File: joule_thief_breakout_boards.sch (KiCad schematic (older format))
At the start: 18 parts, among them J1 Conn_01x02, J10 Conn_01x02, J2 Conn_01x02, J3 Conn_01x02, J4 Conn_01x02, J5 Conn_01x02, J6 Conn_01x03, J7 Conn_01x03, J8 Conn_01x03, J9 Conn_01x02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

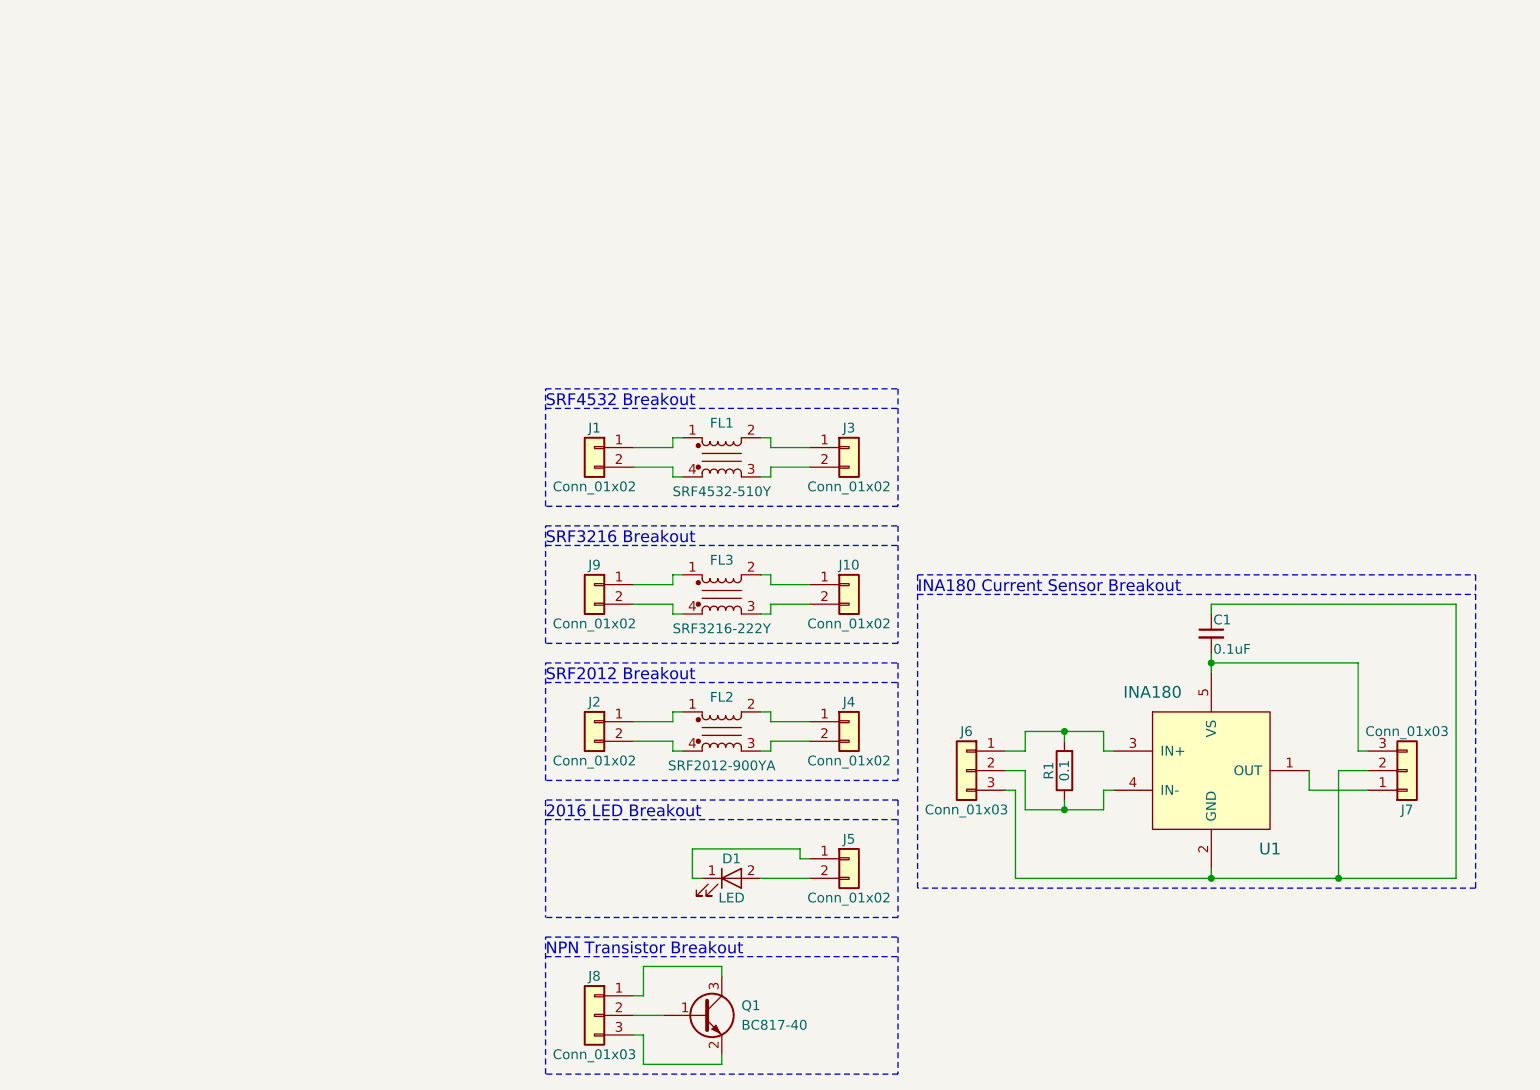
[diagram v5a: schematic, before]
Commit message: add complete joule thief with measurements sensors
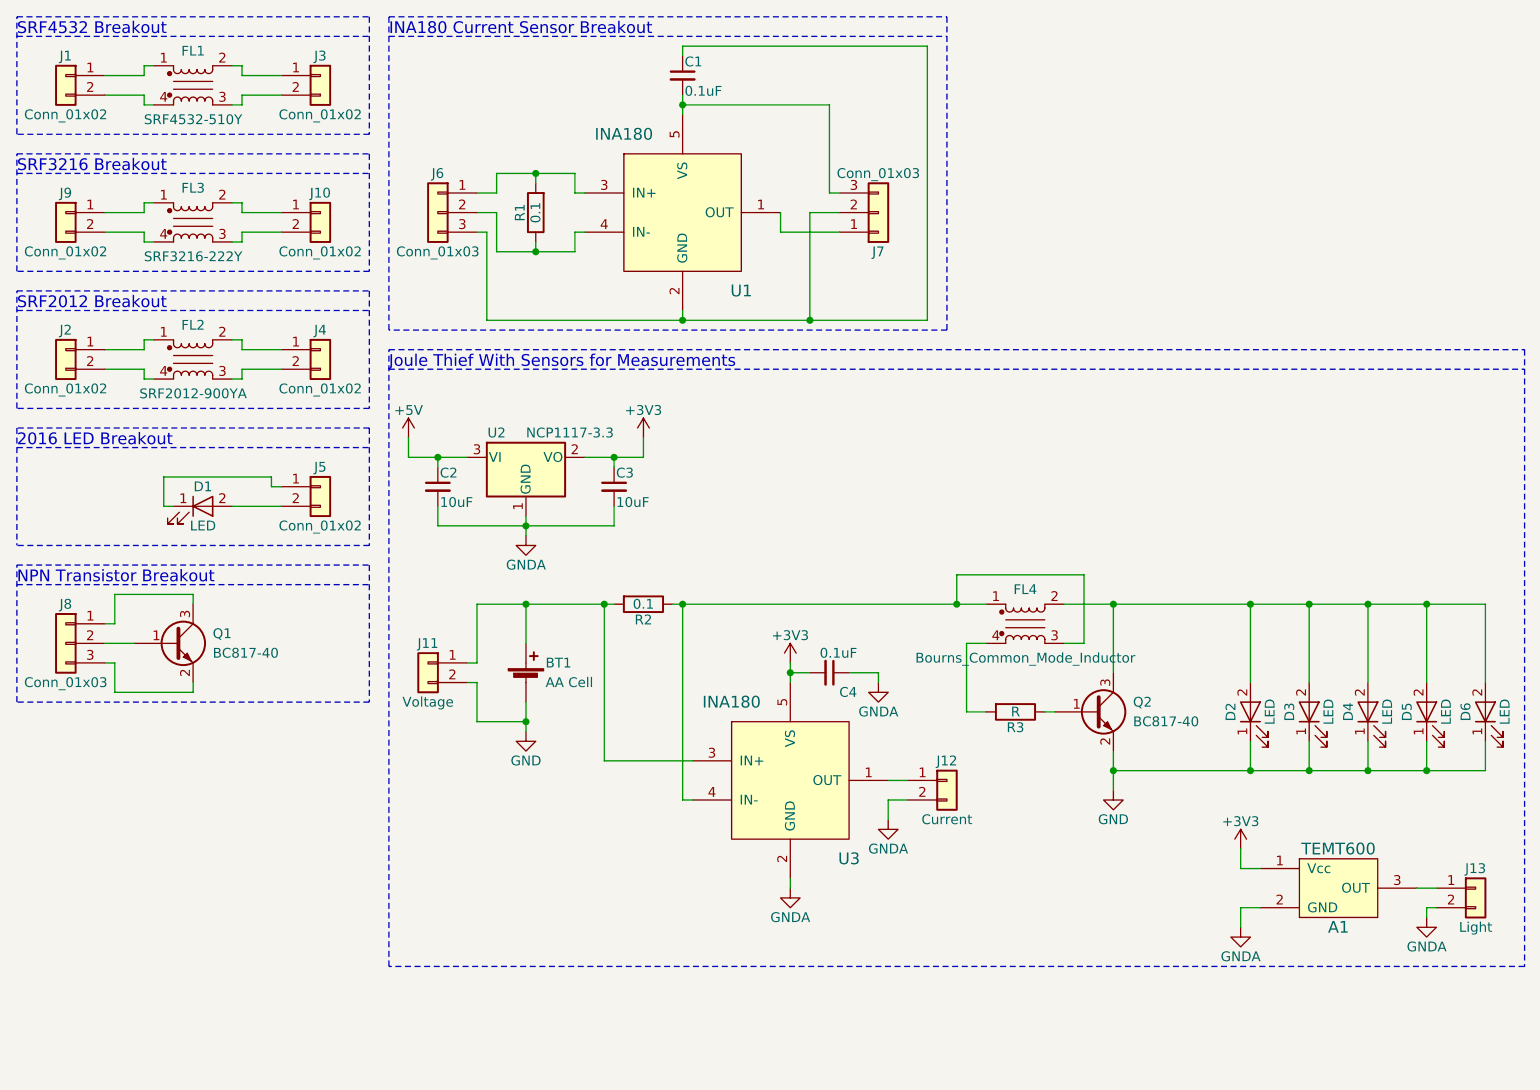
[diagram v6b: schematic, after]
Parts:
- added A1: TEMT600, symbol TEMT600
- added BT1: AA Cell, symbol Battery_Cell
- added C2, C3: 10uF, symbol C_Small
- added C4: 0.1uF, symbol C_Small
- added D2, D3, D4, D5, D6: LED, symbol LED
- added FL4: Bourns_Common_Mode_Inductor, symbol Bourns_Common_Mode_Inductor
- added J11: Voltage, symbol Conn_01x02
- added J12: Current, symbol Conn_01x02
- added J13: Light, symbol Conn_01x02
- added Q2: BC817-40, symbol Q_NPN_BEC
- added R2: 0.1, symbol R
- added R3: R, symbol R
- added U2: NCP1117-3.3, TO_SOT_Packages_SMD:TO-252-2, symbol NCP1117-3.3_TO252
- added U3: INA180, symbol INA180
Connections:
- new net: BT1.1 (+), J11.1 (Pin_1), R2.2, U3.3 (IN+)
- new net: FL4.1, FL4.3, R2.1, U3.4 (IN-)
- new net: D2.2 (A), D3.2 (A), D4.2 (A), D5.2 (A), D6.2 (A), FL4.2, Q2.3 (C)
- new net: FL4.4, R3.2
- new net: Q2.1 (B), R3.1
- new net: J12.1 (Pin_1), U3.1 (OUT)
- new net: A1.3 (OUT), J13.1 (Pin_1)
- new net +3V3: A1.1 (Vcc), C3.1, C4.2, U2.2 (VO), U3.5 (VS)
- new net +5V: C2.1, U2.3 (VI)
- new net GND: BT1.2 (-), D2.1 (K), D3.1 (K), D4.1 (K), D5.1 (K), D6.1 (K), J11.2 (Pin_2), Q2.2 (E)
- new net GNDA: A1.2 (GND), C2.2, C3.2, C4.1, J12.2 (Pin_2), J13.2 (Pin_2), U2.1 (GND), U3.2 (GND)
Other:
- note added: "Joule Thief With Sensors for Measurements"
- moved on the sheet: C1, D1, FL1, FL2, FL3, J1, J10, J2, J3, J4, J5, J6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

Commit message: aa battery clip footprint, assosiate symbols with footprints for sensor joule thief
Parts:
- A1: footprint (none) -> Pin_Headers:Pin_Header_Straight_1x03_Pitch2.54mm
- BT1: footprint (none) -> lib_fp:BK-53_MPD_AAClip
- C2, C3, C4: footprint (none) -> Capacitors_SMD:C_0805_HandSoldering
- D2, D3, D4, D5, D6: footprint (none) -> lib_fp:LED_Luminus_MP-2016
- FL4: footprint (none) -> lib_fp:SRF4532_Bourns_CMI
- J11, J12, J13: footprint (none) -> Pin_Headers:Pin_Header_Straight_2x01_Pitch2.54mm
- Q2: footprint (none) -> TO_SOT_Packages_SMD:SOT-23
- R2, R3: footprint (none) -> Resistors_SMD:R_0805_HandSoldering
- U3: footprint (none) -> TO_SOT_Packages_SMD:TSOT-23-5_HandSoldering
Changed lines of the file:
@@
 F 0 "BT1" H 3300 4100 50  0000 L CNN
 F 1 "AA Cell" H 3300 4000 50  0000 L CNN
-F 2 "" V 3200 4060 50  0001 C CNN
+F 2 "lib_fp:BK-53_MPD_AAClip" V 3200 4060 50  0001 C CNN
 F 3 "" V 3200 4060 50  0001 C CNN
 F 4 "NONE" H 3200 4000 60  0001 C CNN "Manufacture"
@@
 F 0 "FL4" H 5750 3875 50  0000 C CNN
 F 1 "Bourns_Common_Mode_Inductor" H 5750 3525 50  0000 C CNN
-F 2 "" V 5750 3740 50  0000 C CNN
+F 2 "lib_fp:SRF4532_Bourns_CMI" V 5750 3740 50  0001 C CNN
 F 3 "" V 5750 3740 50  0000 C CNN
 	1    5750 3700
@@
 F 0 "Q2" H 6300 4200 50  0000 L CNN
 F 1 "BC817-40" H 6300 4100 50  0000 L CNN
-F 2 "" H 6300 4250 50  0001 C CNN
+F 2 "TO_SOT_Packages_SMD:SOT-23" H 6300 4250 50  0001 C CNN
 F 3 "" H 6100 4150 50  0001 C CNN
 F 4 "NONE" H 6100 4150 60  0001 C CNN "Manufacture"
@@
 F 0 "R3" V 5780 4150 50  0000 C CNN
 F 1 "R" V 5700 4150 50  0000 C CNN
-F 2 "" V 5630 4150 50  0001 C CNN
+F 2 "Resistors_SMD:R_0805_HandSoldering" V 5630 4150 50  0001 C CNN
 F 3 "" H 5700 4150 50  0001 C CNN
 	1    5700 4150
@@
 F 0 "D2" H 6900 4250 50  0000 C CNN
 F 1 "LED" H 6900 4050 50  0000 C CNN
-F 2 "" H 6900 4150 50  0001 C CNN
+F 2 "lib_fp:LED_Luminus_MP-2016" H 6900 4150 50  0001 C CNN
 F 3 "" H 6900 4150 50  0001 C CNN
 	1    6900 4150
@@
 F 0 "D3" H 7200 4250 50  0000 C CNN
 F 1 "LED" H 7200 4050 50  0000 C CNN
-F 2 "" H 7200 4150 50  0001 C CNN
+F 2 "lib_fp:LED_Luminus_MP-2016" H 7200 4150 50  0001 C CNN
 F 3 "" H 7200 4150 50  0001 C CNN
 	1    7200 4150
@@
 F 0 "D4" H 7500 4250 50  0000 C CNN
 F 1 "LED" H 7500 4050 50  0000 C CNN
-F 2 "" H 7500 4150 50  0001 C CNN
+F 2 "lib_fp:LED_Luminus_MP-2016" H 7500 4150 50  0001 C CNN
 F 3 "" H 7500 4150 50  0001 C CNN
 	1    7500 4150
@@
 F 0 "D5" H 7800 4250 50  0000 C CNN
 F 1 "LED" H 7800 4050 50  0000 C CNN
-F 2 "" H 7800 4150 50  0001 C CNN
+F 2 "lib_fp:LED_Luminus_MP-2016" H 7800 4150 50  0001 C CNN
 F 3 "" H 7800 4150 50  0001 C CNN
 	1    7800 4150
@@
 F 0 "D6" H 8100 4250 50  0000 C CNN
 F 1 "LED" H 8100 4050 50  0000 C CNN
-F 2 "" H 8100 4150 50  0001 C CNN
+F 2 "lib_fp:LED_Luminus_MP-2016" H 8100 4150 50  0001 C CNN
 F 3 "" H 8100 4150 50  0001 C CNN
 	1    8100 4150
@@
 F 0 "R2" V 3880 3600 50  0000 C CNN
 F 1 "0.1" V 3800 3600 50  0000 C CNN
-F 2 "" V 3730 3600 50  0001 C CNN
+F 2 "Resistors_SMD:R_0805_HandSoldering" V 3730 3600 50  0001 C CNN
 F 3 "" H 3800 3600 50  0001 C CNN
 F 4 "NONE" H 3800 3600 60  0001 C CNN "Manufacture"
@@
 F 0 "U3" H 4850 4100 60  0000 C CNN
 F 1 "INA180" H 4250 4900 60  0000 C CNN
-F 2 "" H 4550 4500 60  0001 C CNN
+F 2 "TO_SOT_Packages_SMD:TSOT-23-5_HandSoldering" H 4550 4500 60  0001 C CNN
 F 3 "" H 4550 4500 60  0001 C CNN
 	1    4550 4500
@@
 $EndComp
 $Comp
-L GND #PWR3
+L GND #PWR01
 U 1 1 59E32B2A
 P 3200 4250
-F 0 "#PWR3" H 3200 4000 50  0001 C CNN
+F 0 "#PWR01" H 3200 4000 50  0001 C CNN
 F 1 "GND" H 3200 4100 50  0000 C CNN
 F 2 "" H 3200 4250 50  0001 C CNN
@@
 $EndComp
 $Comp
-L GND #PWR9
+L GND #PWR02
 U 1 1 59E32FAB
 P 6200 4550
-F 0 "#PWR9" H 6200 4300 50  0001 C CNN
+F 0 "#PWR02" H 6200 4300 50  0001 C CNN
 F 1 "GND" H 6200 4400 50  0000 C CNN
 F 2 "" H 6200 4550 50  0001 C CNN
@@
 $EndComp
 $Comp
-L +5V #PWR1
+L +5V #PWR03
 U 1 1 59E34F97
 P 2600 2750
-F 0 "#PWR1" H 2600 2600 50  0001 C CNN
+F 0 "#PWR03" H 2600 2600 50  0001 C CNN
 F 1 "+5V" H 2600 2890 50  0000 C CNN
 F 2 "" H 2600 2750 50  0001 C CNN
@@
 F 0 "C2" H 2760 3070 50  0000 L CNN
 F 1 "10uF" H 2760 2920 50  0000 L CNN
-F 2 "" H 2750 3000 50  0001 C CNN
+F 2 "Capacitors_SMD:C_0805_HandSoldering" H 2750 3000 50  0001 C CNN
 F 3 "" H 2750 3000 50  0001 C CNN
 F 4 "NONE" H 2750 3000 60  0001 C CNN "Manufacture"
@@
 F 0 "C3" H 3660 3070 50  0000 L CNN
 F 1 "10uF" H 3660 2920 50  0000 L CNN
-F 2 "" H 3650 3000 50  0001 C CNN
+F 2 "Capacitors_SMD:C_0805_HandSoldering" H 3650 3000 50  0001 C CNN
 F 3 "" H 3650 3000 50  0001 C CNN
 F 4 "NONE" H 3650 3000 60  0001 C CNN "Manufacture"
@@
 $EndComp
 $Comp
-L GNDA #PWR2
+L GNDA #PWR04
 U 1 1 59E35B65
 P 3200 3250
-F 0 "#PWR2" H 3200 3000 50  0001 C CNN
+F 0 "#PWR04" H 3200 3000 50  0001 C CNN
 F 1 "GNDA" H 3200 3100 50  0000 C CNN
 F 2 "" H 3200 3250 50  0001 C CNN
@@
 $EndComp
 $Comp
-L +3V3 #PWR4
+L +3V3 #PWR05
 U 1 1 59E368E8
 P 3800 2750
-F 0 "#PWR4" H 3800 2600 50  0001 C CNN
+F 0 "#PWR05" H 3800 2600 50  0001 C CNN
 F 1 "+3V3" H 3800 2890 50  0000 C CNN
 F 2 "" H 3800 2750 50  0001 C CNN
@@
 $EndComp
 $Comp
-L +3V3 #PWR5
+L +3V3 #PWR06
 U 1 1 59E372B9
 P 4550 3900
-F 0 "#PWR5" H 4550 3750 50  0001 C CNN
+F 0 "#PWR06" H 4550 3750 50  0001 C CNN
 F 1 "+3V3" H 4550 4040 50  0000 C CNN
 F 2 "" H 4550 3900 50  0001 C CNN
@@
 F 0 "C4" V 4850 4000 50  0000 L CNN
 F 1 "0.1uF" V 4650 3900 50  0000 L CNN
-F 2 "" H 4750 3950 50  0001 C CNN
+F 2 "Capacitors_SMD:C_0805_HandSoldering" H 4750 3950 50  0001 C CNN
 F 3 "" H 4750 3950 50  0001 C CNN
 F 4 "NONE" H 4750 3950 60  0001 C CNN "Manufacture"
@@
 $EndComp
 $Comp
-L GNDA #PWR7
+L GNDA #PWR07
 U 1 1 59E378E4
 P 5000 4000
-F 0 "#PWR7" H 5000 3750 50  0001 C CNN
+F 0 "#PWR07" H 5000 3750 50  0001 C CNN
 F 1 "GNDA" H 5000 3850 50  0000 C CNN
 F 2 "" H 5000 4000 50  0001 C CNN
@@
 $EndComp
 $Comp
-L GNDA #PWR6
+L GNDA #PWR08
 U 1 1 59E37D34
 P 4550 5050
-F 0 "#PWR6" H 4550 4800 50  0001 C CNN
+F 0 "#PWR08" H 4550 4800 50  0001 C CNN
 F 1 "GNDA" H 4550 4900 50  0000 C CNN
 F 2 "" H 4550 5050 50  0001 C CNN
@@
 F 0 "J12" H 5350 4600 50  0000 C CNN
 F 1 "Current" H 5350 4300 50  0000 C CNN
-F 2 "" H 5350 4500 50  0001 C CNN
+F 2 "Pin_Headers:Pin_Header_Straight_2x01_Pitch2.54mm" H 5350 4500 50  0001 C CNN
 F 3 "" H 5350 4500 50  0001 C CNN
 F 4 "NONE" H 5350 4500 60  0001 C CNN "Manufacture"
@@
 	5050 4500 5150 4500
 $Comp
-L GNDA #PWR8
+L GNDA #PWR09
 U 1 1 59E3E06D
 P 5050 4700
-F 0 "#PWR8" H 5050 4450 50  0001 C CNN
+F 0 "#PWR09" H 5050 4450 50  0001 C CNN
 F 1 "GNDA" H 5050 4550 50  0000 C CNN
 F 2 "" H 5050 4700 50  0001 C CNN
@@
 F 0 "J11" H 2700 4000 50  0000 C CNN
 F 1 "Voltage" H 2700 3700 50  0000 C CNN
-F 2 "" H 2700 3900 50  0001 C CNN
+F 2 "Pin_Headers:Pin_Header_Straight_2x01_Pitch2.54mm" H 2700 3900 50  0001 C CNN
 F 3 "" H 2700 3900 50  0001 C CNN
 F 4 "NONE" H 2700 3900 60  0001 C CNN "Manufacture"
@@
 F 0 "A1" H 7350 4850 60  0000 C CNN
 F 1 "TEMT600" H 7350 5250 60  0000 C CNN
-F 2 "" H 7350 5050 60  0001 C CNN
+F 2 "Pin_Headers:Pin_Header_Straight_1x03_Pitch2.54mm" H 7350 5050 60  0001 C CNN
 F 3 "" H 7350 5050 60  0001 C CNN
 	1    7350 5050
@@
 $EndComp
 $Comp
-L +3V3 #PWR10
+L +3V3 #PWR010
 U 1 1 59E40E4C
 P 6850 4850
-F 0 "#PWR10" H 6850 4700 50  0001 C CNN
+F 0 "#PWR010" H 6850 4700 50  0001 C CNN
 F 1 "+3V3" H 6850 4990 50  0000 C CNN
 F 2 "" H 6850 4850 50  0001 C CNN
@@
 	6850 4950 6950 4950
 $Comp
-L GNDA #PWR11
+L GNDA #PWR011
 U 1 1 59E41141
 P 6850 5250
-F 0 "#PWR11" H 6850 5000 50  0001 C CNN
+F 0 "#PWR011" H 6850 5000 50  0001 C CNN
 F 1 "GNDA" H 6850 5100 50  0000 C CNN
 F 2 "" H 6850 5250 50  0001 C CNN
@@
 F 0 "J13" H 8050 5150 50  0000 C CNN
 F 1 "Light" H 8050 4850 50  0000 C CNN
-F 2 "" H 8050 5050 50  0001 C CNN
+F 2 "Pin_Headers:Pin_Header_Straight_2x01_Pitch2.54mm" H 8050 5050 50  0001 C CNN
 F 3 "" H 8050 5050 50  0001 C CNN
 F 4 "NONE" H 8050 5050 60  0001 C CNN "Manufacture"
@@
 	7750 5050 7850 5050
 $Comp
-L GNDA #PWR12
+L GNDA #PWR012
 U 1 1 59E4170F
 P 7800 5200
-F 0 "#PWR12" H 7800 4950 50  0001 C CNN
+F 0 "#PWR012" H 7800 4950 50  0001 C CNN
 F 1 "GNDA" H 7800 5050 50  0000 C CNN
 F 2 "" H 7800 5200 50  0001 C CNN
